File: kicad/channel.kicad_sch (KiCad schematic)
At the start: 34 parts, among them J1 Conn_01x02_Pin, J2 Conn_01x02_Pin, J3 Conn_01x02_Pin, U4 MCP23017_SP, U6 MAX7219

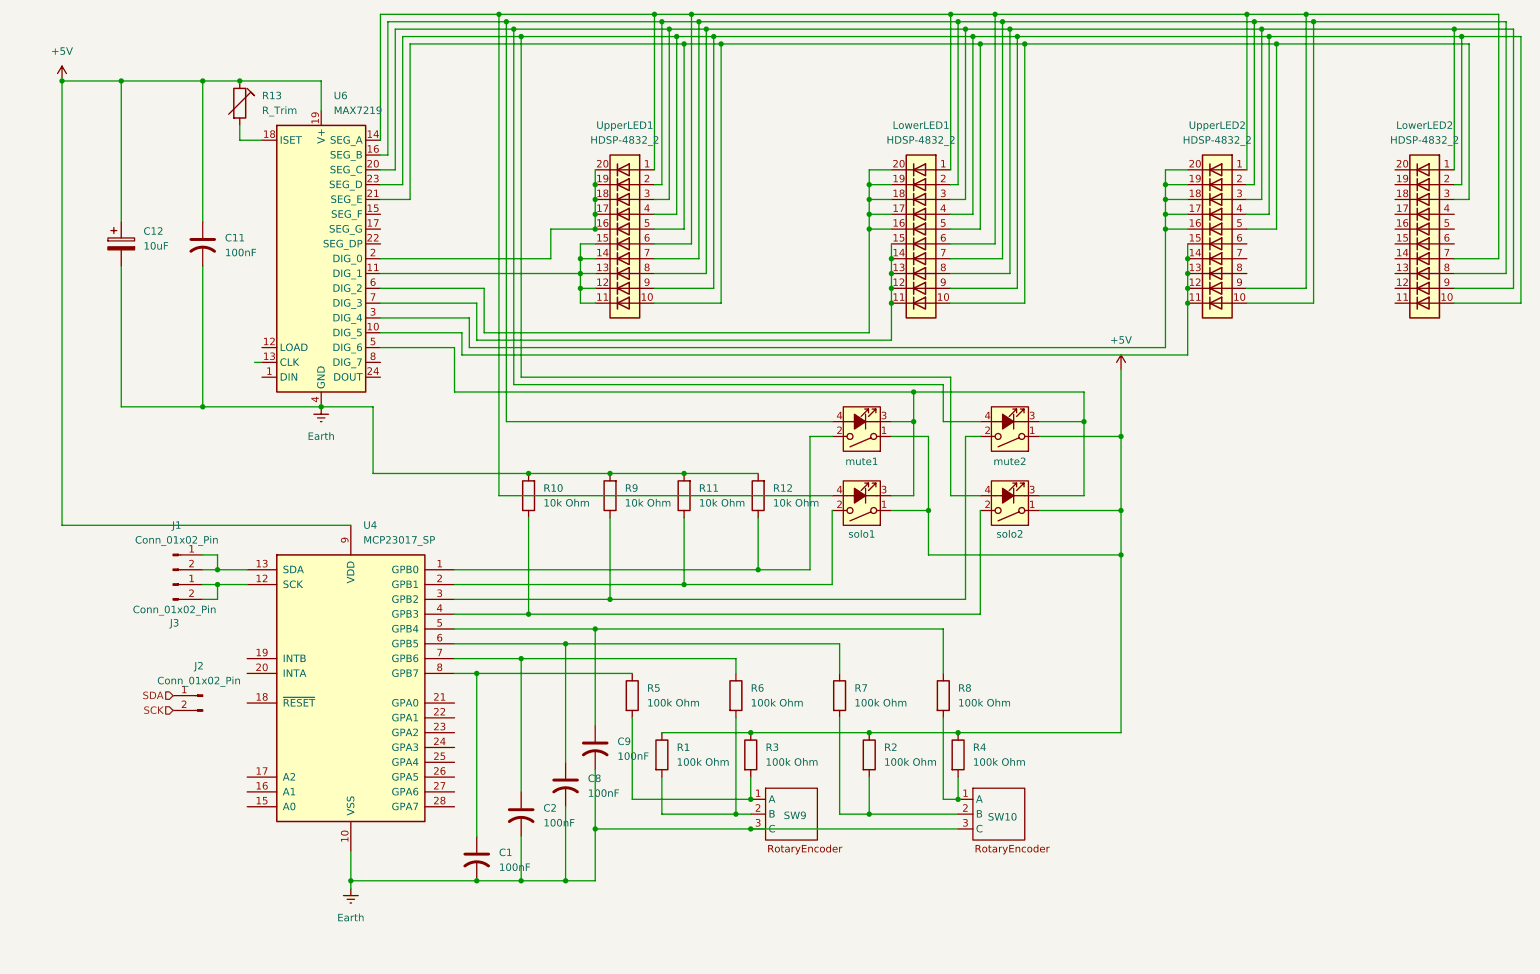
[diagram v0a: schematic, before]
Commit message: mcp23017 circuit update
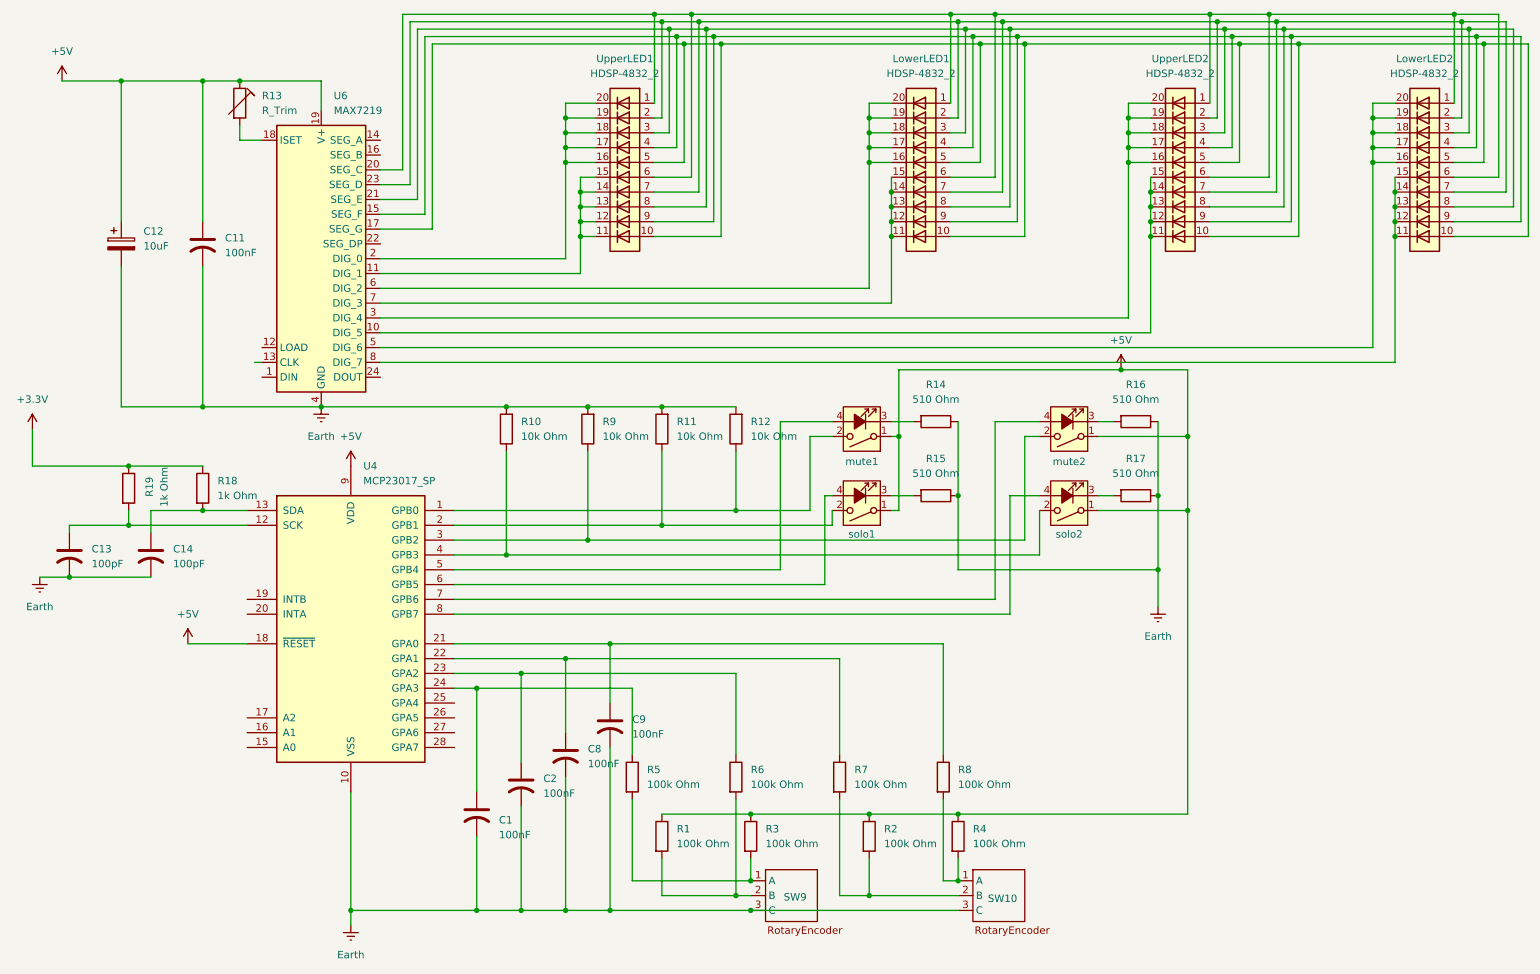
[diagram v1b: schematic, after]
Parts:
- removed J1, J2, J3: Conn_01x02_Pin, symbol Connector:Conn_01x02_Pin
- added C13, C14: 100pF, symbol Device:C_US
- added R14, R15, R16, R17: 510 Ohm, symbol Device:R
- added R18, R19: 1k Ohm, symbol Device:R
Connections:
- net +5V: now also U4.18 (~{RESET})
- net Earth: now also C13.2, C14.2, R14.1, R15.1, R16.1, R17.1
- net at U4.12 (SCK): now also C13.1, R19.2
- net at U4.13 (SDA): now also C14.1, R18.2
- net at U4.21 (GPA0): now also C9.1, R8.1
- net at U4.22 (GPA1): now also C8.1, R7.1
- net at U4.23 (GPA2): now also C2.1, R6.1
- net at U4.24 (GPA3): now also C1.1, R5.1
- net at LowerLED1.3 (A), LowerLED1.8 (A), UpperLED1.3 (A)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: now also LowerLED2.3 (A), LowerLED2.8 (A), U6.21 (SEG_E), UpperLED2.8 (A); no longer LowerLED2.1 (A), LowerLED2.9 (A), U6.20 (SEG_C), mute2.4 (A)
- net at LowerLED1.4 (A), LowerLED1.9 (A), UpperLED1.4 (A)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: now also LowerLED2.4 (A), LowerLED2.9 (A), U6.15 (SEG_F), UpperLED2.9 (A); no longer LowerLED2.10 (A), LowerLED2.2 (A), U6.23 (SEG_D), solo2.4 (A)
- net at LowerLED2.11 (K): now also LowerLED2.12 (K), LowerLED2.13 (K), LowerLED2.14 (K), LowerLED2.15 (K), U6.8 (DIG_7)
- net at LowerLED2.16 (K): now also LowerLED2.17 (K), LowerLED2.18 (K), LowerLED2.19 (K), LowerLED2.20 (K), U6.5 (DIG_6)
- net at LowerLED1.10 (A), LowerLED1.5 (A), UpperLED1.10 (A)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: now also LowerLED2.10 (A), LowerLED2.5 (A), U6.17 (SEG_G), UpperLED2.10 (A); no longer LowerLED2.3 (A), U6.21 (SEG_E)
- net at LowerLED2.6 (A): now also LowerLED1.1 (A), LowerLED1.6 (A), LowerLED2.1 (A), U6.20 (SEG_C), UpperLED1.1 (A), UpperLED1.6 (A), UpperLED2.1 (A), UpperLED2.6 (A)
- net at LowerLED1.2 (A), LowerLED1.7 (A), UpperLED1.2 (A)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: now also LowerLED2.2 (A), LowerLED2.7 (A), U6.23 (SEG_D), UpperLED2.7 (A); no longer LowerLED2.8 (A), U6.16 (SEG_B), UpperLED2.10 (A), mute1.4 (A)
- new net: R14.2, mute1.3 (K)
- new net: U4.5 (GPB4), mute1.4 (A)
- new net: U4.6 (GPB5), solo1.4 (A)
- new net: U4.7 (GPB6), mute2.4 (A)
- new net: U4.8 (GPB7), solo2.4 (A)
- new net: R17.2, solo2.3 (K)
- new net: R16.2, mute2.3 (K)
- new net: R15.2, solo1.3 (K)
- new net +3.3V: R18.1, R19.1
- now unconnected: U6.14 (SEG_A)
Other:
- moved on the sheet: C1, C2, C8, C9, LowerLED1, LowerLED2, R1, R10, R11, R12, R2, R3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

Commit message: fix max7219 init
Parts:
- added R20: 1k Ohm, symbol Device:R
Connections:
- net +5V: now also U4.17 (A2), R20.1
- net Earth: now also R20.2
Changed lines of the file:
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@@
 	)
 	(junction
+		(at 46.99 142.24)
+		(diameter 0)
+		(color 0 0 0 0)
+	)
+	(junction
 		(at 129.54 88.9)
 		(diameter 0)
@@
 	(wire
 		(pts
+			(xy 36.83 142.24) (xy 46.99 142.24)
+		)
+		(stroke
+			(width 0)
+			(type default)
+		)
+	)
+	(wire
+		(pts
 			(xy 81.28 63.5) (xy 113.03 63.5)
 		)
@@
 	(wire
 		(pts
+			(xy 46.99 142.24) (xy 58.42 142.24)
+		)
+		(stroke
+			(width 0)
+			(type default)
+		)
+	)
+	(wire
+		(pts
 			(xy 57.15 40.64) (xy 57.15 43.18)
 		)
@@
 	)
 	(symbol
+		(lib_id "power:Earth")
+		(at 46.99 149.86 0)
+		(unit 1)
+		(exclude_from_sim no)
+		(in_bom yes)
+		(on_board yes)
+		(dnp no)
+		(fields_autoplaced yes)
+		(property "Reference" "#PWR019"
+			(at 46.99 156.21 0)
+			(effects
+				(font
+					(size 1.27 1.27)
+				)
+				(hide yes)
+			)
+		)
+		(property "Value" "Earth"
+			(at 46.99 154.94 0)
+			(effects
+				(font
+					(size 1.27 1.27)
+				)
+			)
+		)
+		(property "Footprint" ""
+			(at 46.99 149.86 0)
+			(effects
+				(font
+					(size 1.27 1.27)
+				)
+				(hide yes)
+			)
+		)
+		(property "Datasheet" "~"
+			(at 46.99 149.86 0)
+			(effects
+				(font
+					(size 1.27 1.27)
+				)
+				(hide yes)
+			)
+		)
+		(property "Description" "Power symbol creates a global label with name \"Earth\""
+			(at 46.99 149.86 0)
+			(effects
+				(font
+					(size 1.27 1.27)
+				)
+				(hide yes)
+			)
+		)
+		(pin "1"
+		)
+		(instances
+			(project "mixer"
+				(path "/d102195a-4964-4d79-a57c-1abf3bee20c0/096db37f-e53c-4de1-ba52-3c444b492505"
+					(reference "#PWR019")
+					(unit 1)
+				)
+			)
+		)
+	)
+	(symbol
 		(lib_id "Device:R")
 		(at 176.53 91.44 270)
@@
 	)
 	(symbol
+		(lib_id "Device:R")
+		(at 46.99 146.05 0)
+		(unit 1)
+		(exclude_from_sim no)
+		(in_bom yes)
+		(on_board yes)
+		(dnp no)
+		(property "Reference" "R20"
+			(at 50.546 145.796 90)
+			(effects
+				(font
+					(size 1.27 1.27)
+				)
+			)
+		)
+		(property "Value" "1k Ohm"
+			(at 53.086 145.796 90)
+			(effects
+				(font
+					(size 1.27 1.27)
+				)
+			)
+		)
+		(property "Footprint" ""
+			(at 45.212 146.05 90)
+			(effects
+				(font
+					(size 1.27 1.27)
+				)
+				(hide yes)
+			)
+		)
+		(property "Datasheet" "~"
+			(at 46.99 146.05 0)
+			(effects
+				(font
+					(size 1.27 1.27)
+				)
+				(hide yes)
+			)
+		)
+		(property "Description" "Resistor"
+			(at 46.99 146.05 0)
+			(effects
+				(font
+					(size 1.27 1.27)
+				)
+				(hide yes)
+			)
+		)
+		(pin "2"
+		)
+		(pin "1"
+		)
+		(instances
+			(project "mixer"
+				(path "/d102195a-4964-4d79-a57c-1abf3bee20c0/096db37f-e53c-4de1-ba52-3c444b492505"
+					(reference "R20")
+					(unit 1)
+				)
+			)
+		)
+	)
+	(symbol
 		(lib_id "power:+5V")
 		(at 208.28 82.55 0)
@@
 					(unit 1)
 				)
+			)
+		)
+	)
+	(symbol
+		(lib_id "power:+5V")
+		(at 36.83 142.24 0)
+		(unit 1)
+		(exclude_from_sim no)
+		(in_bom yes)
+		(on_board yes)
+		(dnp no)
+		(fields_autoplaced yes)
+		(property "Reference" "#PWR018"
+			(at 36.83 146.05 0)
+			(effects
+				(font
+					(size 1.27 1.27)
+				)
+				(hide yes)
+			)
+		)
+		(property "Value" "+5V"
+			(at 36.83 137.16 0)
+			(effects
+				(font
+					(size 1.27 1.27)
+				)
+			)
+		)
+		(property "Footprint" ""
+			(at 36.83 142.24 0)
+			(effects
+				(font
+					(size 1.27 1.27)
+				)
+				(hide yes)
+			)
+		)
+		(property "Datasheet" ""
+			(at 36.83 142.24 0)
+			(effects
+				(font
+					(size 1.27 1.27)
+				)
+				(hide yes)
+			)
+		)
+		(property "Description" "Power symbol creates a global label with name \"+5V\""
+			(at 36.83 142.24 0)
+			(effects
+				(font
+					(size 1.27 1.27)
+				)
+				(hide yes)
+			)
+		)
+		(pin "1"
+		)
+		(instances
+			(project "mixer"
+				(path "/d102195a-4964-4d79-a57c-1abf3bee20c0/096db37f-e53c-4de1-ba52-3c444b492505"
+					(reference "#PWR018")
+					(unit 1)
+				)

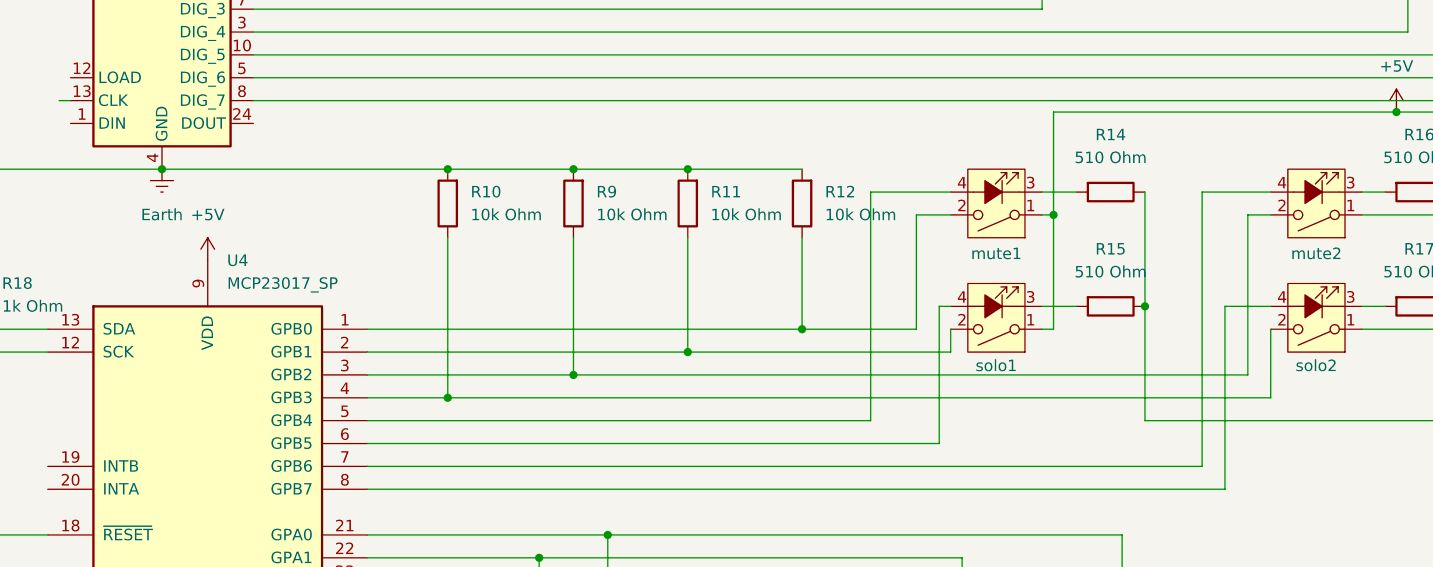
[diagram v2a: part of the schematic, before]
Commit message: mcp23017 interrupts
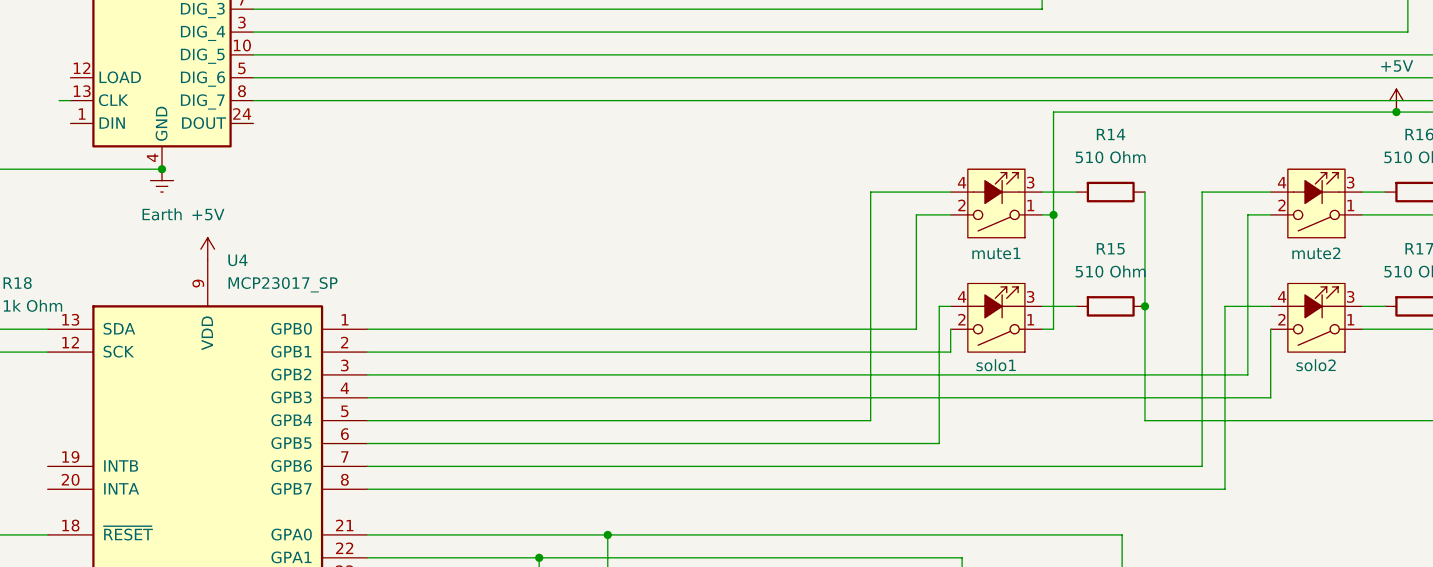
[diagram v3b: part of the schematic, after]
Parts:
- removed R10, R11, R12, R9: 10k Ohm, symbol Device:R
